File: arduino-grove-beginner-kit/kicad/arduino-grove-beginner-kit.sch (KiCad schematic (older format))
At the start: 0 parts

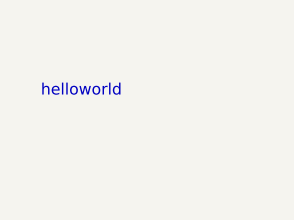
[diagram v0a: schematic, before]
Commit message: update simple button for arduino-grove,
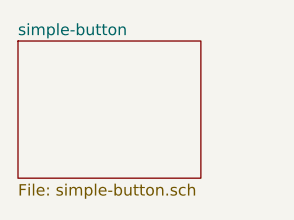
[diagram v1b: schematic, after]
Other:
- note removed: "helloworld"
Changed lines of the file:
@@
 $Descr User 5846 4134
 encoding utf-8
-Sheet 1 1
+Sheet 1 2
 Title ""
 Date ""
@@
 Comment4 ""
 $EndDescr
-Text Notes 700  900  0    50   ~ 0
-helloworld
+$Sheet
+S 600  650  800  600
+U 5F3C13C2
+F0 "simple-button" 50
+F1 "simple-button.sch" 50
+$EndSheet
 $EndSCHEMATC
